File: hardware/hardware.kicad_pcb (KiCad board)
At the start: 2 copper layers, 62.6 x 68.5 mm, 9 parts, among them J1 Conn_01x02, SW1 SW_Push, SW2 SW_Push, SW3 SW_Push, SW4 SW_SPDT, U2 XIAO-nRF54l15-SMD

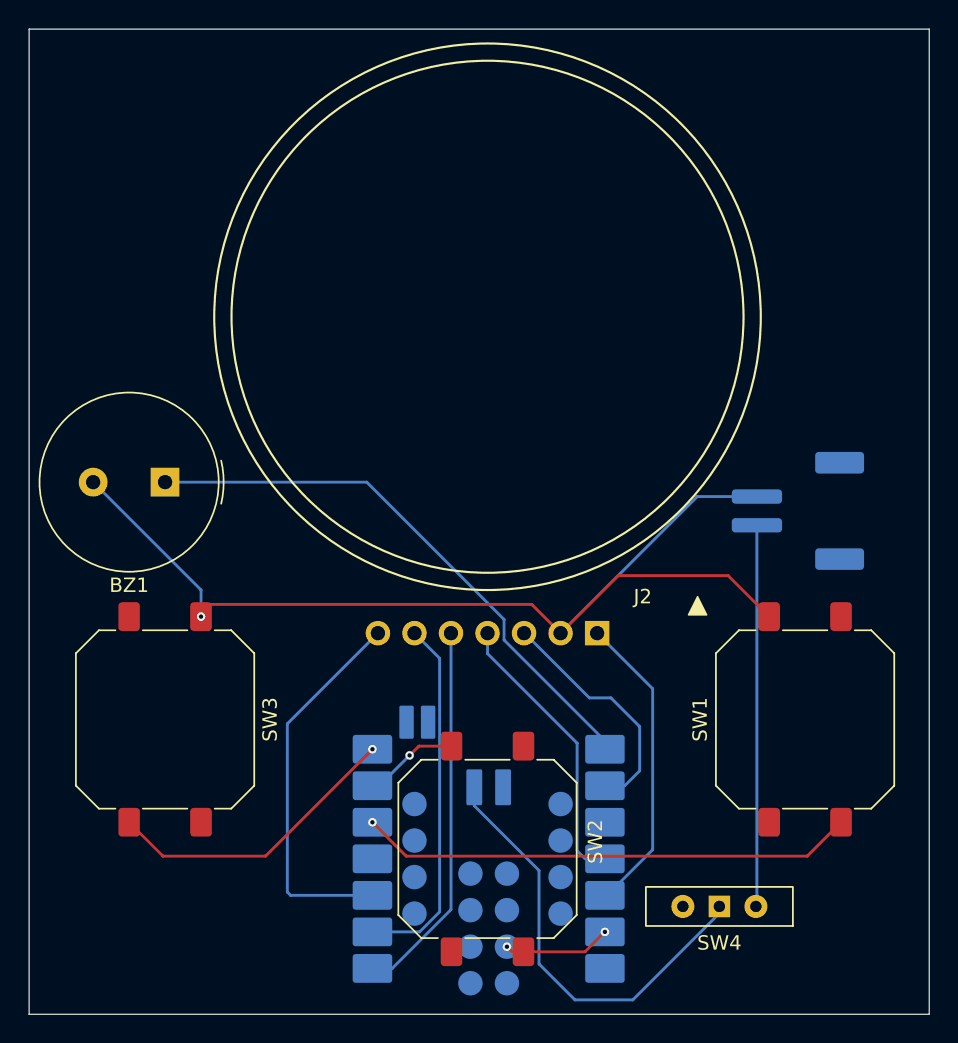
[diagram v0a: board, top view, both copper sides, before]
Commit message: Define PCB stackup and bump trace width to 0.381mm
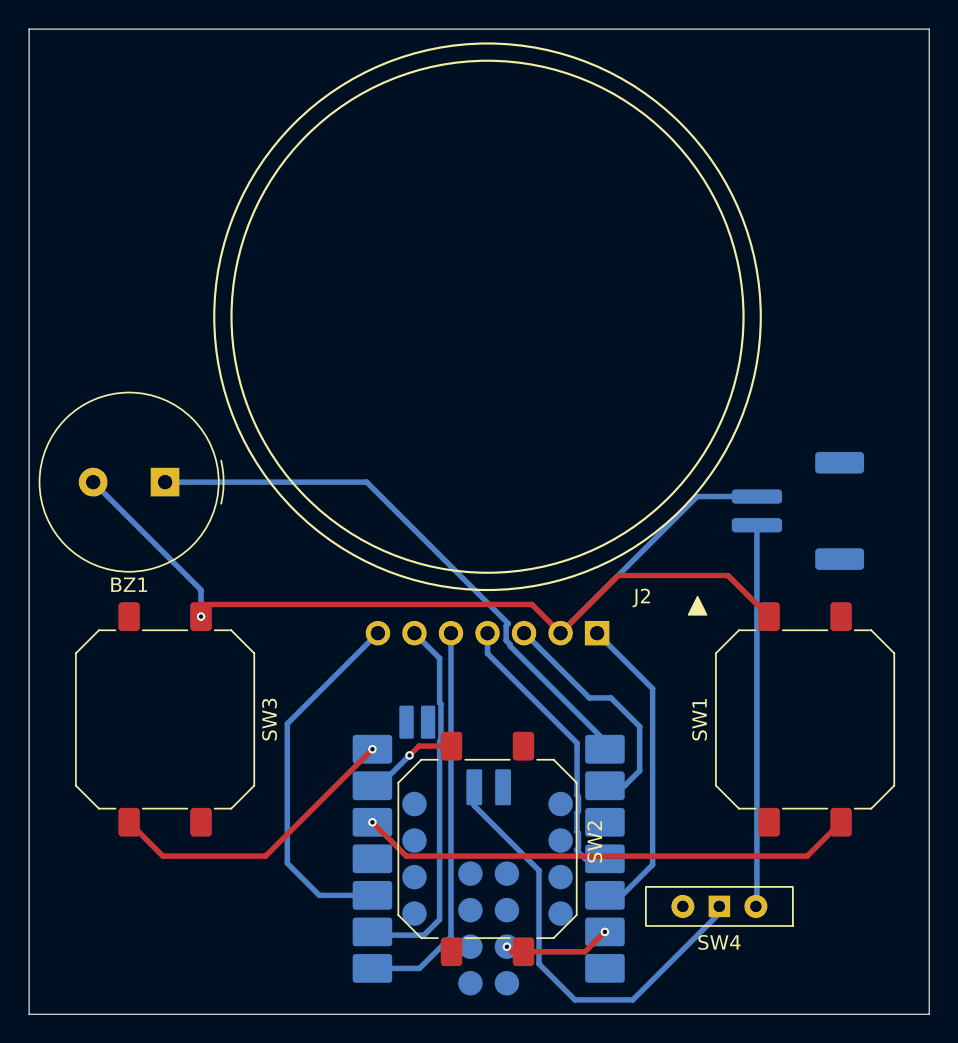
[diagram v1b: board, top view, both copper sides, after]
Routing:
- net Net-(J2-RST): track 26.6 -> 25.4 mm
- net Net-(J2-DC): track 26.4 -> 27.5 mm
- net Net-(J2-VCC): track 21.3 -> 21.9 mm
- net Net-(J2-CS): track 25.4 -> 25.9 mm
